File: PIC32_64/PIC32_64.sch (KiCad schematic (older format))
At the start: 20 parts, among them P1 CONN_8X2, P2 CONN_8X2, P3 CONN_8X2, P4 CONN_8X2, U1 PIC32MX795F512H, X1 8Mhz

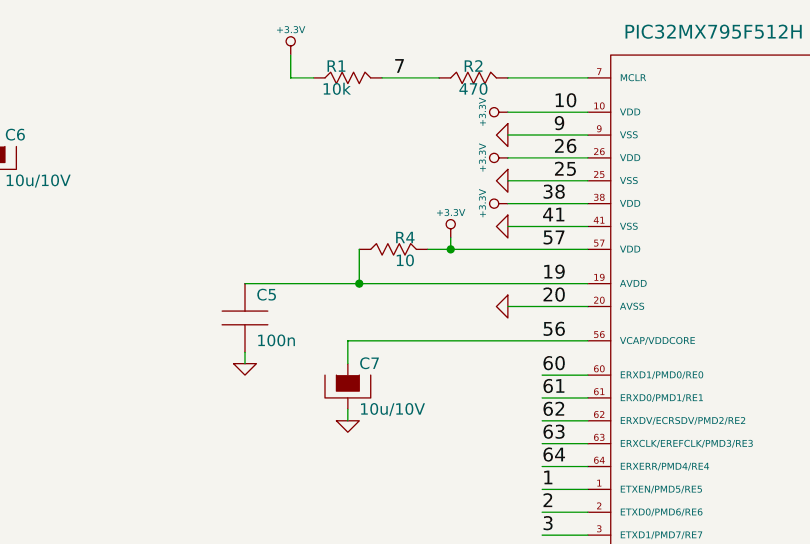
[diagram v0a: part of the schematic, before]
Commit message: Ajout valeurs composants
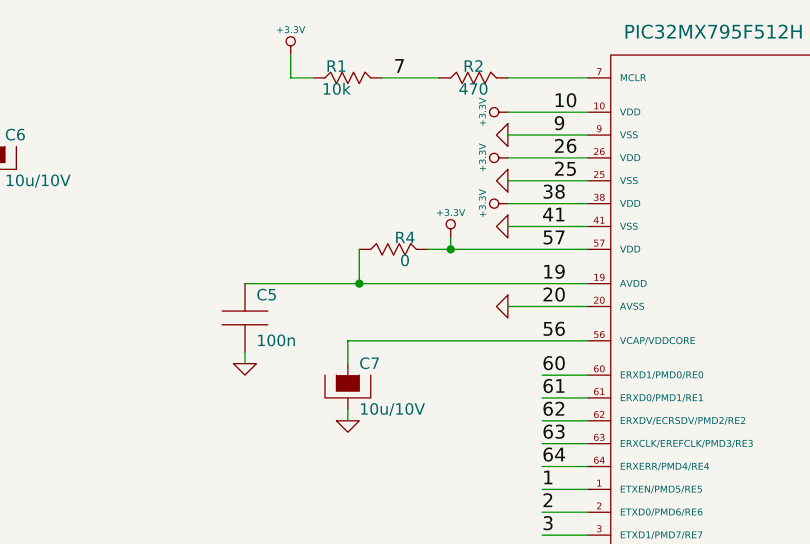
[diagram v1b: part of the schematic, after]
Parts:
- R4: value 10 -> 0
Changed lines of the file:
@@
-EESchema Schematic File Version 2  date 05/06/2012 00:05:48
+EESchema Schematic File Version 2  date 11/06/2012 23:06:50
 LIBS:power
 LIBS:CEN-SCHEMA
-LIBS:PIC32_64-cache
 EELAYER 25  0
 EELAYER END
@@
 Sheet 1 1
 Title "SO100"
-Date "4 jun 2012"
+Date "11 jun 2012"
 Rev "V1-00"
 Comp "CYBERNETIQUE EN NORD"
@@
 P 6000 2550
 F 0 "R4" V 5950 2500 50  0000 C CNN
-F 1 "10" V 6050 2500 50  0000 C CNN
+F 1 "0" V 6050 2500 50  0000 C CNN
 	1    6000 2550
 	0    1    1    0

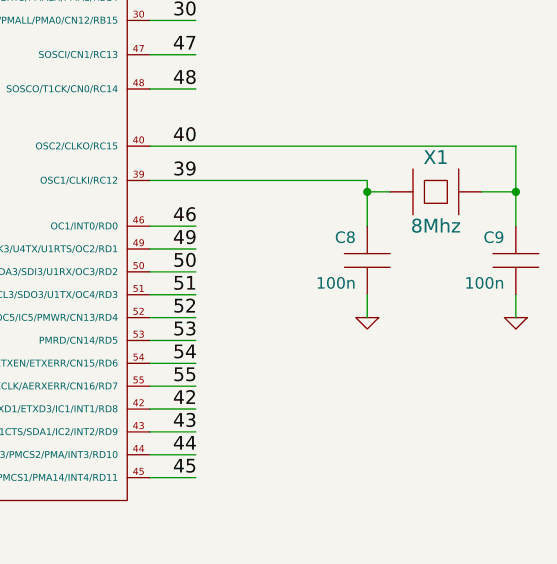
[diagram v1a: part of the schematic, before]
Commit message: modif valeur composant
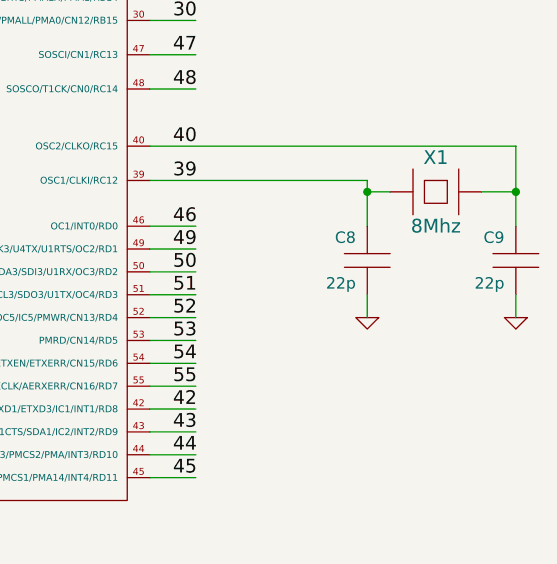
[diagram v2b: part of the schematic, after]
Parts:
- C8, C9: value 100n -> 22p
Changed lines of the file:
@@
-EESchema Schematic File Version 2  date 11/06/2012 23:06:50
+EESchema Schematic File Version 2  date 24/08/2012 17:26:21
 LIBS:power
 LIBS:CEN-SCHEMA
@@
 Sheet 1 1
 Title "SO100"
-Date "11 jun 2012"
+Date "24 aug 2012"
 Rev "V1-00"
 Comp "CYBERNETIQUE EN NORD"
@@
 P 10250 4350
 F 0 "C8" H 10300 4450 50  0000 L CNN
-F 1 "100n" H 10300 4250 50  0000 L CNN
+F 1 "22p" H 10300 4250 50  0000 L CNN
 	1    10250 4350
 	-1   0    0    -1
@@
 P 10900 4350
 F 0 "C9" H 10950 4450 50  0000 L CNN
-F 1 "100n" H 10950 4250 50  0000 L CNN
+F 1 "22p" H 10950 4250 50  0000 L CNN
 	1    10900 4350
 	-1   0    0    -1
